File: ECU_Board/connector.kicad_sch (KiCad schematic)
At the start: 2 parts, among them J1 Conn_02x20_Odd_Even, J2 Conn_01x02

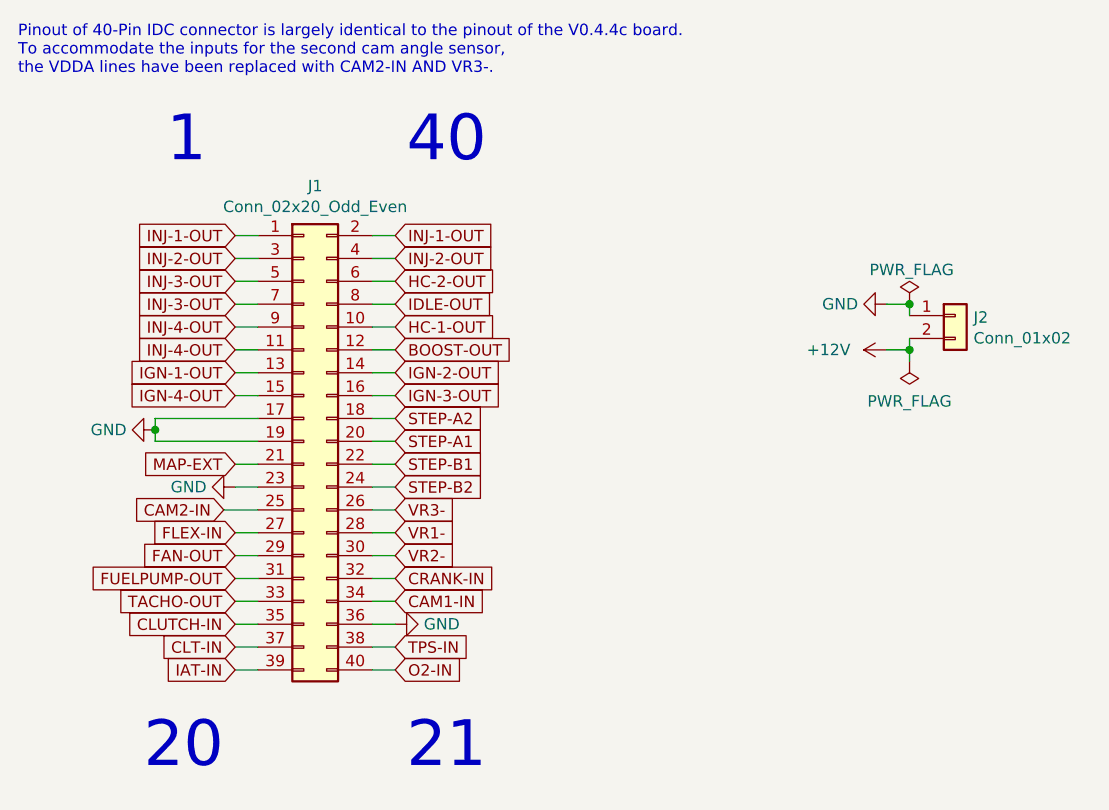
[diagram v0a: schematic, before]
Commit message: Removed clutch input
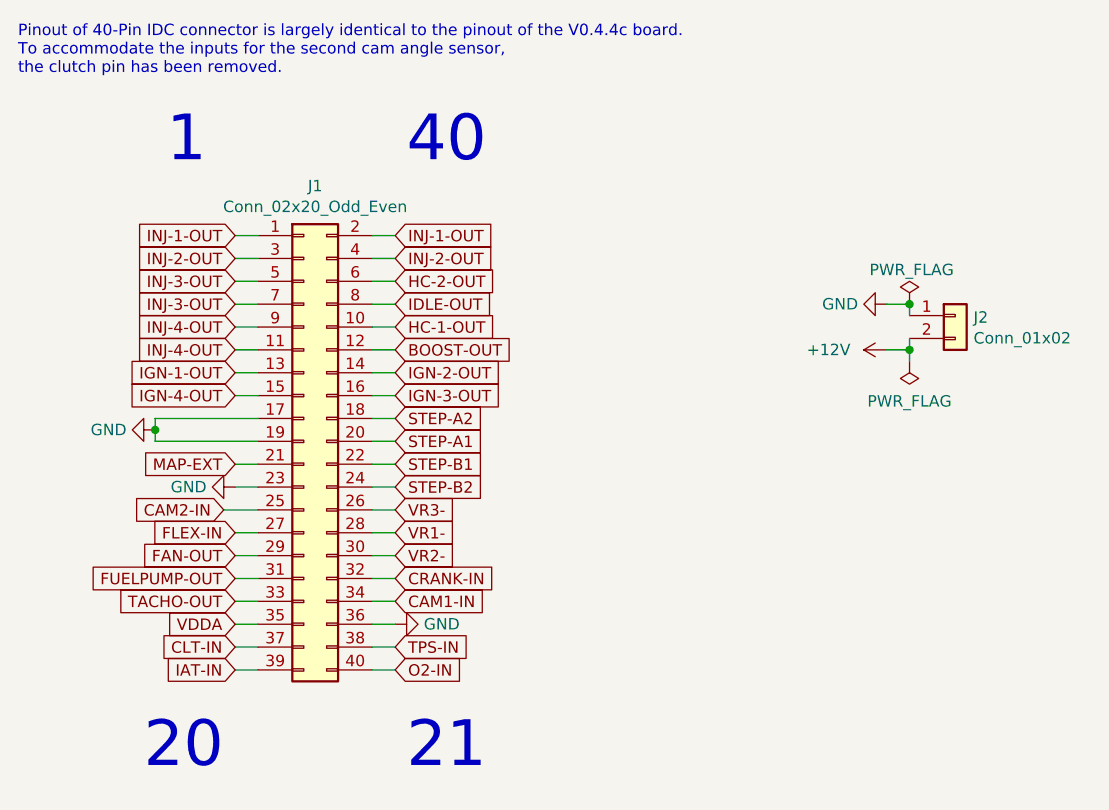
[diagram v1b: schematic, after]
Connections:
- net CLUTCH-IN renamed VDDA
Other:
- note added: "Pinout of 40-Pin IDC connector is largely identical to the pinout of the V0.4.4c board. To accommodate the inputs for the second cam angle sensor, the clutch pin has been removed."
- note removed: "Pinout of 40-Pin IDC connector is largely identical to the pinout of the V0.4.4c board. To accommodate the inputs for the second cam angle sensor, the VDDA lines have been replaced with CAM2-IN AND VR3-."
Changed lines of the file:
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@@
   (title_block
     (title "Speeduino board for Teensy 4.1")
-    (date "2023-01-02")
-    (rev "5")
+    (date "2023-01-07")
+    (rev "6")
     (company "Fontys Eindhoven EXPO group 13 || Speeduino")
     (comment 1 "Adapted from Speeduino V0.4.4c board")
@@
     (effects (font (size 5.08 5.08)) (justify left bottom))
   )
-  (text "Pinout of 40-Pin IDC connector is largely identical to the pinout of the V0.4.4c board.\nTo accommodate the inputs for the second cam angle sensor, \nthe VDDA lines have been replaced with CAM2-IN AND VR3-."
+  (text "Pinout of 40-Pin IDC connector is largely identical to the pinout of the V0.4.4c board.\nTo accommodate the inputs for the second cam angle sensor,\nthe clutch pin has been removed."
     (at 123.19 55.88 0)
     (effects (font (size 1.27 1.27)) (justify left bottom))
@@
     )
   )
-  (global_label "CLUTCH-IN" (shape input) (at 147.32 116.84 180) (fields_autoplaced)
-    (effects (font (size 1.27 1.27)) (justify right))
-    (property "Intersheet References" "${INTERSHEET_REFS}" (id 0) (at 134.2026 116.7606 0)
-      (effects (font (size 1.27 1.27)) (justify right) hide)
-    )
-  )
   (global_label "IGN-1-OUT" (shape input) (at 147.32 88.9 180) (fields_autoplaced)
     (effects (font (size 1.27 1.27)) (justify right))
@@
     )
   )
+  (global_label "VDDA" (shape input) (at 147.32 116.84 180) (fields_autoplaced)
+    (effects (font (size 1.27 1.27)) (justify right))
+    (property "Intersheet References" "${INTERSHEET_REFS}" (id 0) (at 140.1898 116.7606 0)
+      (effects (font (size 1.27 1.27)) (justify right) hide)
+    )
+  )

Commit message: Changed Boost output to ACIS
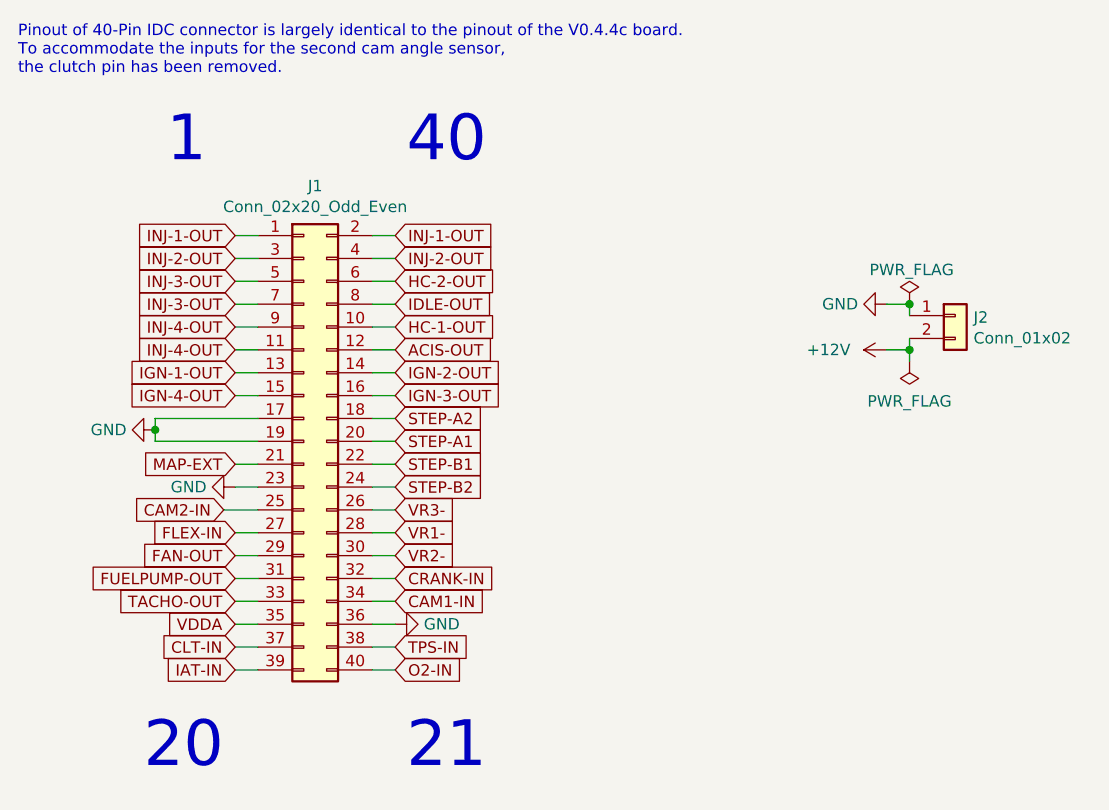
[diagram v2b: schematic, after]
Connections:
- net BOOST-OUT renamed ACIS-OUT
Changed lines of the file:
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@@
     )
   )
-  (global_label "BOOST-OUT" (shape input) (at 165.1 86.36 0) (fields_autoplaced)
+  (global_label "ACIS-OUT" (shape input) (at 165.1 86.36 0) (fields_autoplaced)
     (effects (font (size 1.27 1.27)) (justify left))
-    (property "Intersheet References" "${INTERSHEET_REFS}" (id 0) (at 0 0 0)
-      (effects (font (size 1.27 1.27)) hide)
+    (property "Intersheet References" "${INTERSHEET_REFS}" (id 0) (at 176.8869 86.2806 0)
+      (effects (font (size 1.27 1.27)) (justify left) hide)
     )
   )

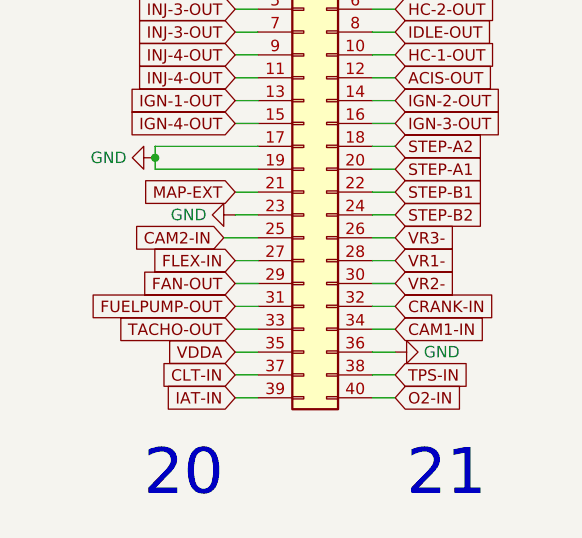
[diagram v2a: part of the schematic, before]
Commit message: Finished adapter board, slight changes to ECU
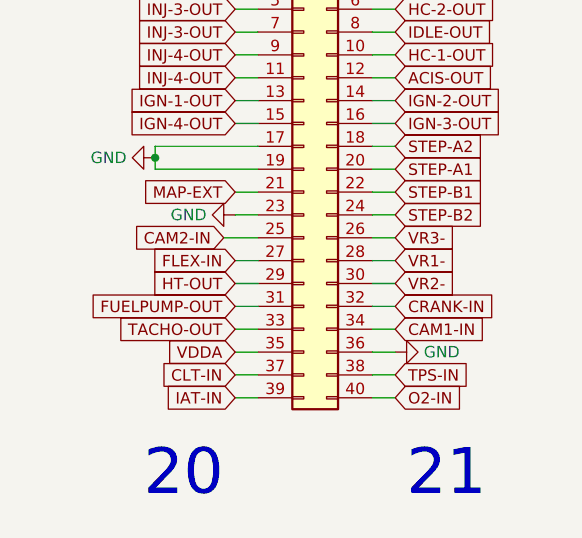
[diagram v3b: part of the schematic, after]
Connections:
- net FAN-OUT renamed HT-OUT
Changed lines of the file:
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@@
     )
   )
-  (global_label "FAN-OUT" (shape input) (at 147.32 109.22 180) (fields_autoplaced)
+  (global_label "HT-OUT" (shape input) (at 147.32 109.22 180) (fields_autoplaced)
     (effects (font (size 1.27 1.27)) (justify right))
-    (property "Intersheet References" "${INTERSHEET_REFS}" (id 0) (at 26.67 3.81 0)
-      (effects (font (size 1.27 1.27)) hide)
+    (property "Intersheet References" "${INTERSHEET_REFS}" (id 0) (at 137.4079 109.1406 0)
+      (effects (font (size 1.27 1.27)) (justify right) hide)
     )
   )
